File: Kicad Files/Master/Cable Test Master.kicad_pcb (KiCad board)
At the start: 2 copper layers, 50.8 x 61.6 mm, 64 parts, among them J1 RJ45, J2 RJ12, J3 PWR, J4 ISP, Q1 BSS84, Q10 2N7002, Q11 2N7002, Q12 2N7002, Q13 2N7002, Q14 2N7002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

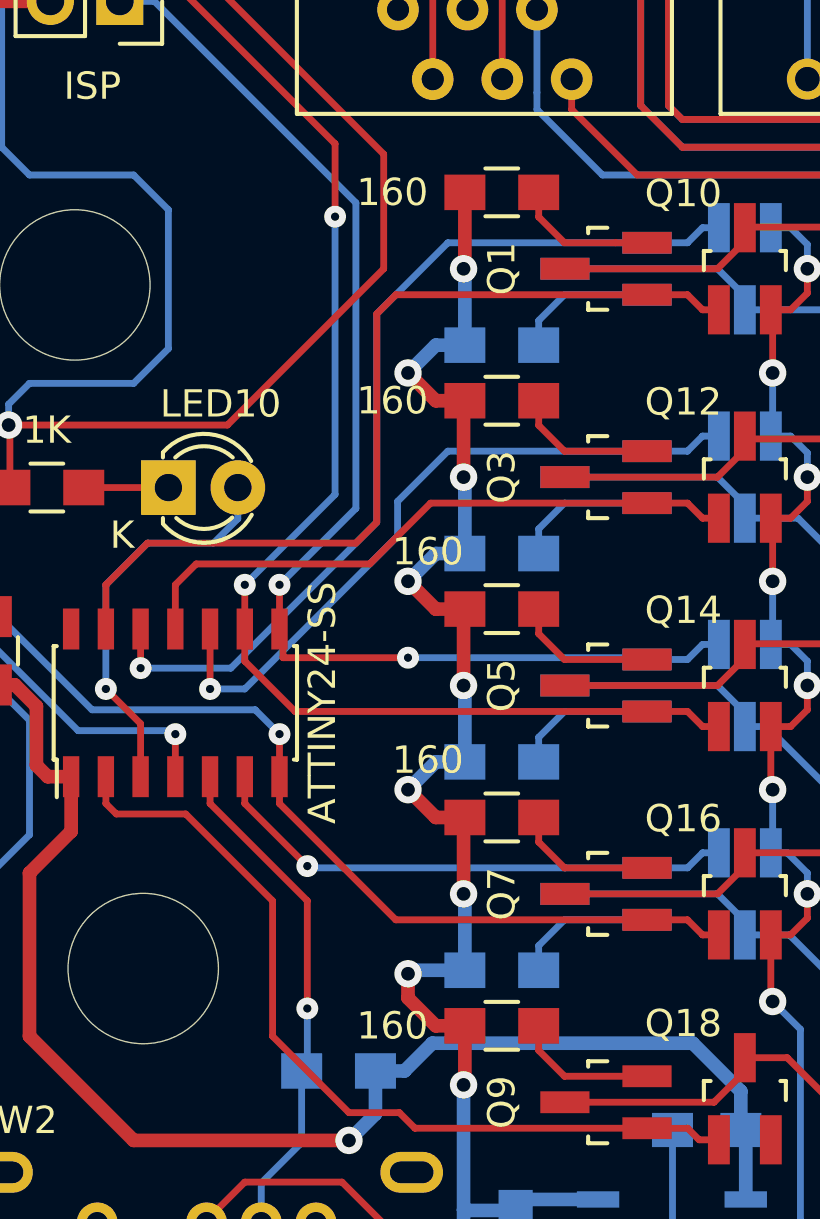
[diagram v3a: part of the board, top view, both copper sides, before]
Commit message: Change R1-R9 to 100 ohm
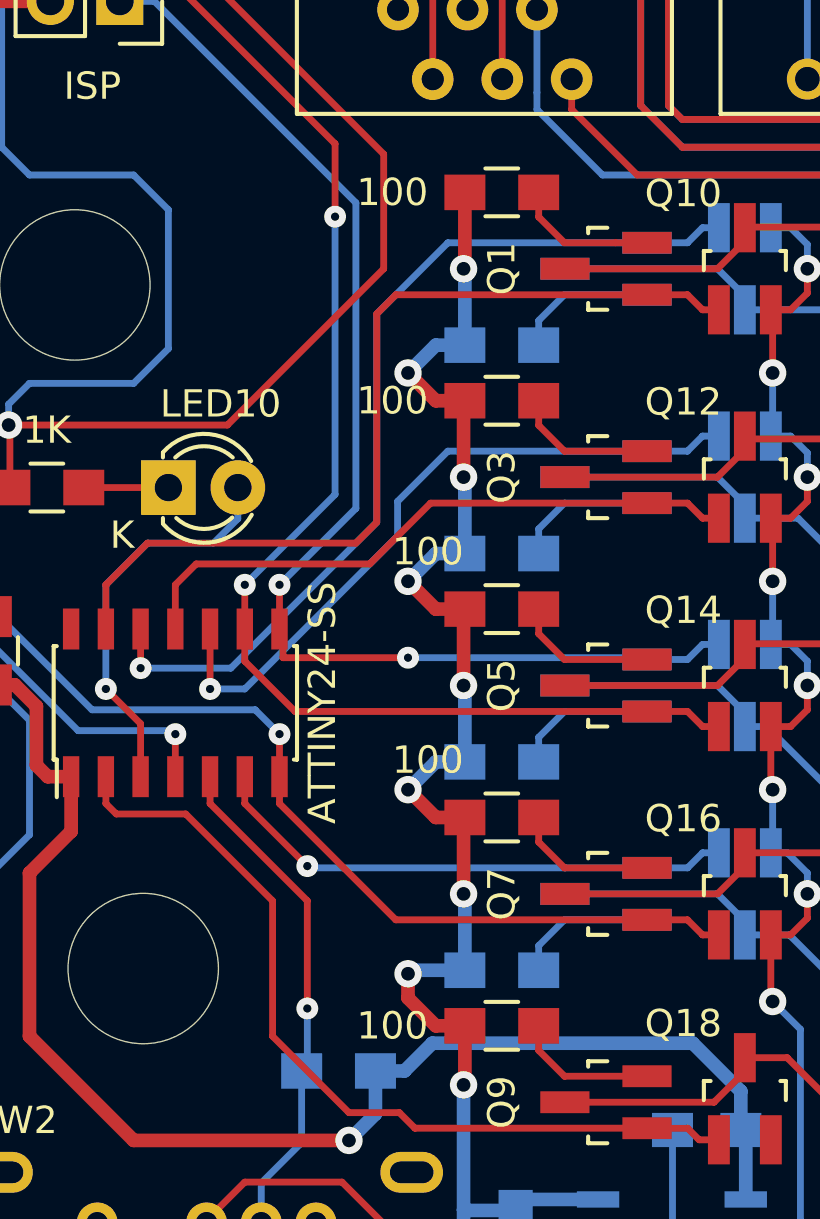
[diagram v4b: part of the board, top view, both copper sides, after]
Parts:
- R1, R2, R3, R4, R5, R6, R7, R8, R9: value 160 -> 100
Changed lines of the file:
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@@
     (links 131)
     (no_connects 0)
-    (area 105.560536 62.0022 166.084524 129.25044)
+    (area 111.684999 63.424999 162.635001 125.170001)
     (thickness 1.6)
     (drawings 10)
@@
       (effects (font (size 1 1) (thickness 0.15)))
     )
-    (fp_text value 160 (at -4 0) (layer F.SilkS)
+    (fp_text value 100 (at -4 0) (layer F.SilkS)
       (effects (font (size 1 1) (thickness 0.15)))
     )
@@
       (effects (font (size 1 1) (thickness 0.15)) (justify mirror))
     )
-    (fp_text value 160 (at -4 0) (layer B.SilkS)
+    (fp_text value 100 (at -4 0) (layer B.SilkS)
       (effects (font (size 1 1) (thickness 0.15)) (justify mirror))
     )
@@
       (effects (font (size 1 1) (thickness 0.15)))
     )
-    (fp_text value 160 (at -4 0) (layer F.SilkS)
+    (fp_text value 100 (at -4 0) (layer F.SilkS)
       (effects (font (size 1 1) (thickness 0.15)))
     )
@@
       (effects (font (size 1 1) (thickness 0.15)) (justify mirror))
     )
-    (fp_text value 160 (at -4 0) (layer B.SilkS)
+    (fp_text value 100 (at -4 0) (layer B.SilkS)
       (effects (font (size 1 1) (thickness 0.15)) (justify mirror))
     )
@@
       (effects (font (size 1 1) (thickness 0.15)))
     )
-    (fp_text value 160 (at -2.7 -2.1) (layer F.SilkS)
+    (fp_text value 100 (at -2.7 -2.1) (layer F.SilkS)
       (effects (font (size 1 1) (thickness 0.15)))
     )
@@
       (effects (font (size 1 1) (thickness 0.15)) (justify mirror))
     )
-    (fp_text value 160 (at -4 0) (layer B.SilkS)
+    (fp_text value 100 (at -4 0) (layer B.SilkS)
       (effects (font (size 1 1) (thickness 0.15)) (justify mirror))
     )
@@
       (effects (font (size 1 1) (thickness 0.15)))
     )
-    (fp_text value 160 (at -2.7 -2.1) (layer F.SilkS)
+    (fp_text value 100 (at -2.7 -2.1) (layer F.SilkS)
       (effects (font (size 1 1) (thickness 0.15)))
     )
@@
       (effects (font (size 1 1) (thickness 0.15)) (justify mirror))
     )
-    (fp_text value 160 (at -4 0) (layer B.SilkS)
+    (fp_text value 100 (at -4 0) (layer B.SilkS)
       (effects (font (size 1 1) (thickness 0.15)) (justify mirror))
     )
@@
       (effects (font (size 1 1) (thickness 0.15)))
     )
-    (fp_text value 160 (at -4 0) (layer F.SilkS)
-      (effects (font (size 1 1) (thickness 0.15)))
-    )
+    (fp_text value 100 (at -4 0) (layer F.SilkS)
+      (effects (font (size 1 1) (thickness 0.15)))
+    )

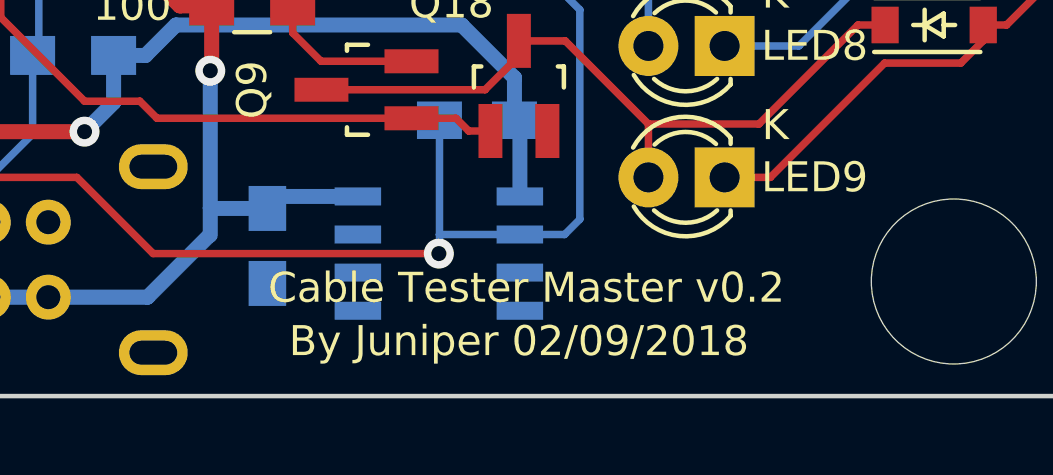
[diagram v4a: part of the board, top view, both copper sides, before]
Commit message: Fix revision printing on PCB
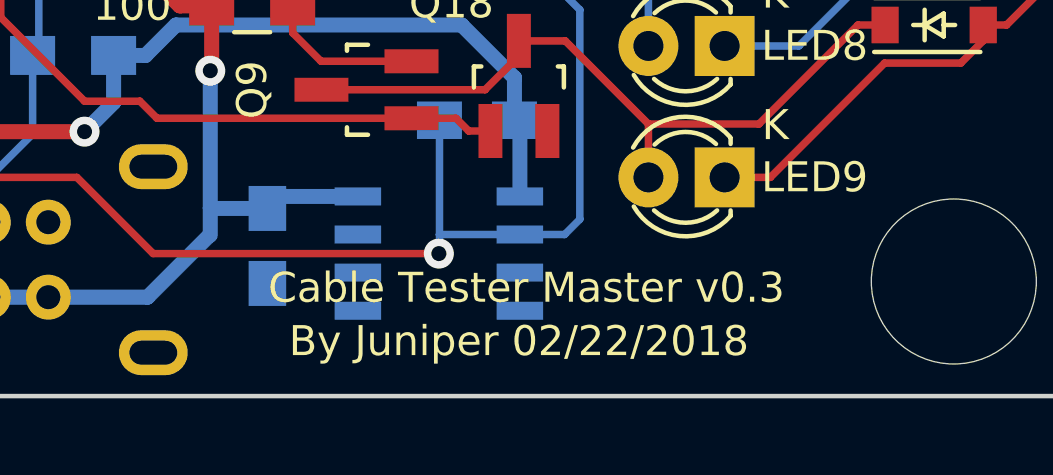
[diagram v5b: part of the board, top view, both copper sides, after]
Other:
- board text added: "By Juniper 02/22/2018"
- board text added: "Cable Tester Master v0.3"
- board text removed: "By Juniper 02/09/2018"
- board text removed: "Cable Tester Master v0.2"
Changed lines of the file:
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@@
     (links 131)
     (no_connects 0)
-    (area 111.684999 63.424999 162.635001 125.170001)
+    (area 105.560536 62.0022 166.084524 129.25044)
     (thickness 1.6)
     (drawings 10)
@@
   (gr_arc (start 161.925 64.135) (end 161.925 63.5) (angle 90) (layer Edge.Cuts) (width 0.15))
   (gr_arc (start 112.395 64.135) (end 111.76 64.135) (angle 90) (layer Edge.Cuts) (width 0.15))
-  (gr_text "By Juniper 02/09/2018" (at 143.002 123.2662) (layer F.SilkS)
+  (gr_text "By Juniper 02/22/2018" (at 143.002 123.2662) (layer F.SilkS)
     (effects (font (size 1 1) (thickness 0.2)))
   )
-  (gr_text "Cable Tester Master v0.2" (at 143.256 121.4882) (layer F.SilkS)
+  (gr_text "Cable Tester Master v0.3" (at 143.256 121.4882) (layer F.SilkS)
     (effects (font (size 1 1) (thickness 0.2)))
   )

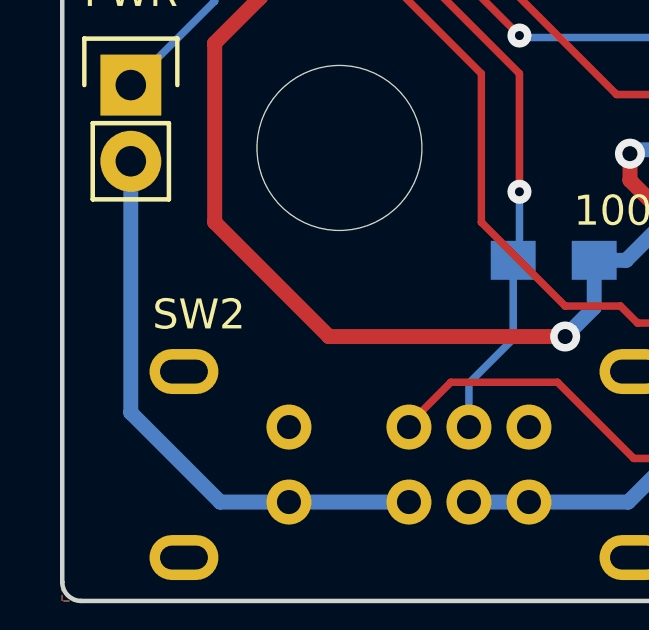
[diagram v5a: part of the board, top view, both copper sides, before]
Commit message: Change SW2 reference to SW1
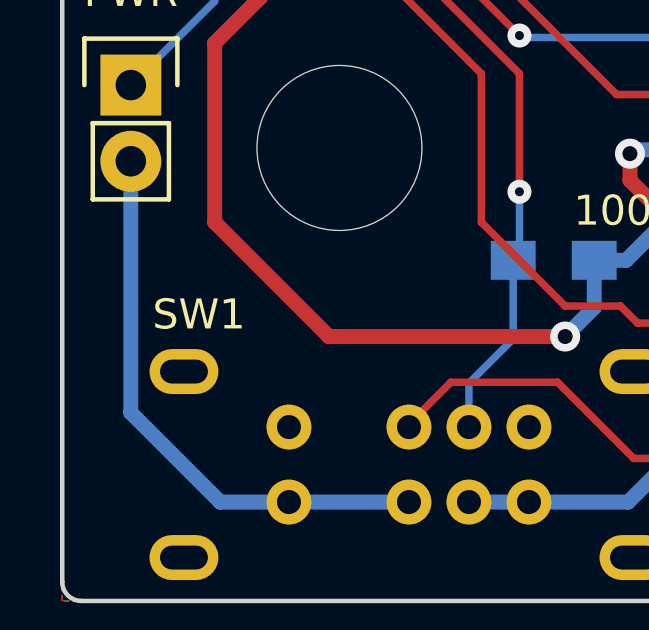
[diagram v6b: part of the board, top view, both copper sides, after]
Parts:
- removed SW2: DP3T, Tester Switches:SW_DP3T_SLIDE
- added SW1: DP3T, Tester Switches:SW_DP3T_SLIDE, F.Cu at (123.3, 120.5)

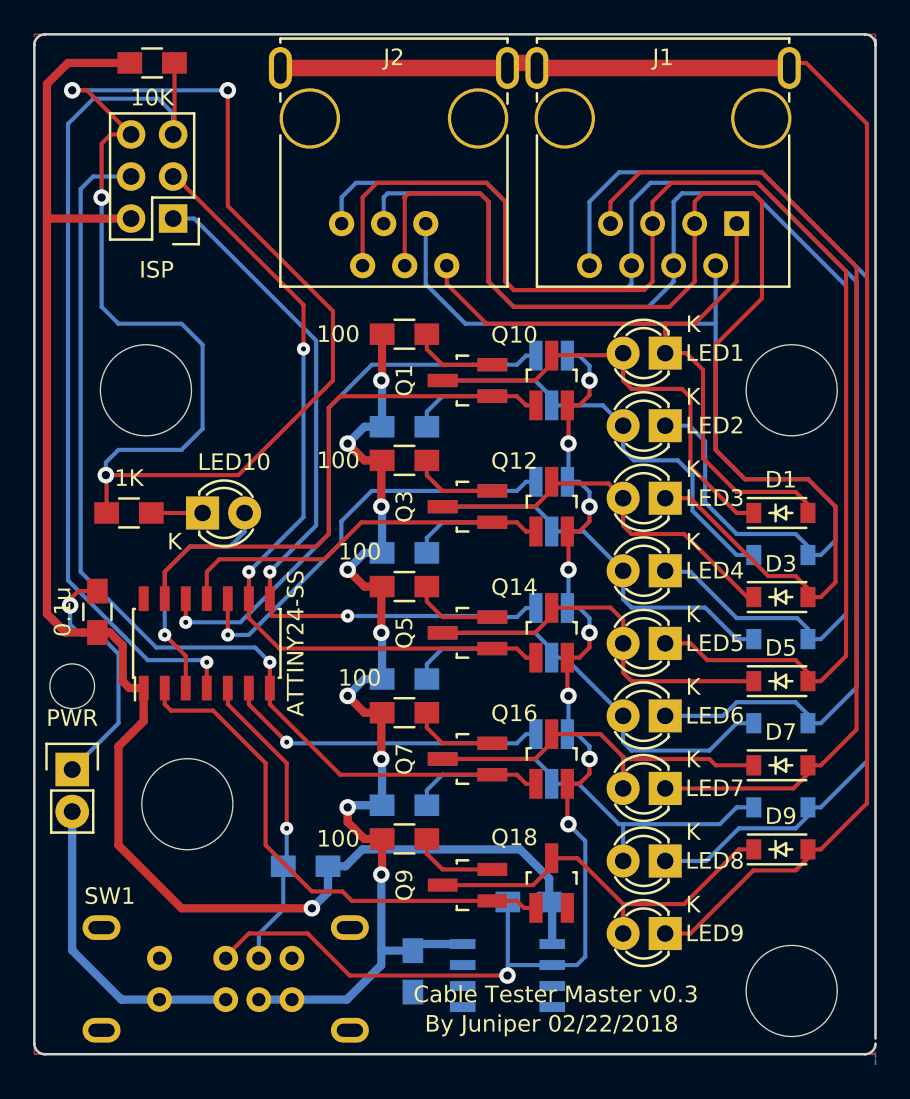
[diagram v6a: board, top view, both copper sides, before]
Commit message: Change current limiting resistors to 200 Ohm
The 100 Ohm resistors worked but the LEDs burn rather bright. Increasing resistance to be easier on eyes. Also changed BOM to match.
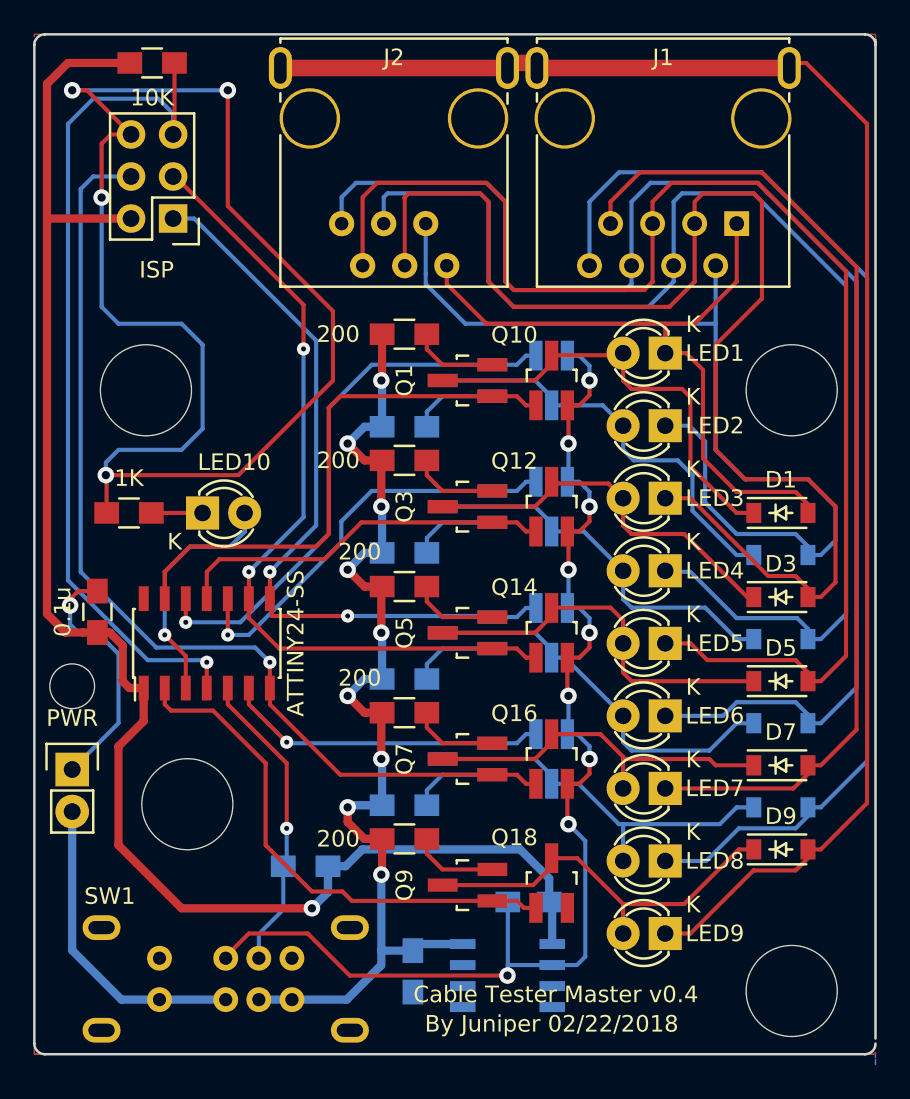
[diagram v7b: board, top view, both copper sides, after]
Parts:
- R1, R2, R3, R4, R5, R6, R7, R8, R9: value 100 -> 200
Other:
- board text added: "Cable Tester Master v0.4"
- board text removed: "Cable Tester Master v0.3"
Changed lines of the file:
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@@
 (kicad_pcb (version 4) (host pcbnew 4.0.2+dfsg1-stable)
   (general
-    (links 138)
-    (no_connects 7)
+    (links 131)
+    (no_connects 0)
     (area 111.684999 63.424999 162.635001 125.170001)
     (thickness 1.6)
@@
     (add_net "Net-(R12-Pad2)")
     (add_net "Net-(SW1-Pad5)")
-    (add_net "Net-(SW2-Pad5)")
     (add_net VCC)
   )
@@
       (effects (font (size 1 1) (thickness 0.15)))
     )
-    (fp_text value 100 (at -4 0) (layer F.SilkS)
+    (fp_text value 200 (at -4 0) (layer F.SilkS)
       (effects (font (size 1 1) (thickness 0.15)))
     )
@@
       (effects (font (size 1 1) (thickness 0.15)) (justify mirror))
     )
-    (fp_text value 100 (at -4 0) (layer B.SilkS)
+    (fp_text value 200 (at -4 0) (layer B.SilkS)
       (effects (font (size 1 1) (thickness 0.15)) (justify mirror))
     )
@@
       (effects (font (size 1 1) (thickness 0.15)))
     )
-    (fp_text value 100 (at -4 0) (layer F.SilkS)
+    (fp_text value 200 (at -4 0) (layer F.SilkS)
       (effects (font (size 1 1) (thickness 0.15)))
     )
@@
       (effects (font (size 1 1) (thickness 0.15)) (justify mirror))
     )
-    (fp_text value 100 (at -4 0) (layer B.SilkS)
+    (fp_text value 200 (at -4 0) (layer B.SilkS)
       (effects (font (size 1 1) (thickness 0.15)) (justify mirror))
     )
@@
       (effects (font (size 1 1) (thickness 0.15)))
     )
-    (fp_text value 100 (at -2.7 -2.1) (layer F.SilkS)
+    (fp_text value 200 (at -2.7 -2.1) (layer F.SilkS)
       (effects (font (size 1 1) (thickness 0.15)))
     )
@@
       (effects (font (size 1 1) (thickness 0.15)) (justify mirror))
     )
-    (fp_text value 100 (at -4 0) (layer B.SilkS)
+    (fp_text value 200 (at -4 0) (layer B.SilkS)
       (effects (font (size 1 1) (thickness 0.15)) (justify mirror))
     )
@@
       (effects (font (size 1 1) (thickness 0.15)))
     )
-    (fp_text value 100 (at -2.7 -2.1) (layer F.SilkS)
+    (fp_text value 200 (at -2.7 -2.1) (layer F.SilkS)
       (effects (font (size 1 1) (thickness 0.15)))
     )
@@
       (effects (font (size 1 1) (thickness 0.15)) (justify mirror))
     )
-    (fp_text value 100 (at -4 0) (layer B.SilkS)
+    (fp_text value 200 (at -4 0) (layer B.SilkS)
       (effects (font (size 1 1) (thickness 0.15)) (justify mirror))
     )
@@
       (effects (font (size 1 1) (thickness 0.15)))
     )
-    (fp_text value 100 (at -4 0) (layer F.SilkS)
+    (fp_text value 200 (at -4 0) (layer F.SilkS)
       (effects (font (size 1 1) (thickness 0.15)))
     )
@@
     (effects (font (size 1 1) (thickness 0.2)))
   )
-  (gr_text "Cable Tester Master v0.3" (at 143.256 121.4882) (layer F.SilkS)
+  (gr_text "Cable Tester Master v0.4" (at 143.256 121.4882) (layer F.SilkS)
     (effects (font (size 1 1) (thickness 0.2)))
   )
